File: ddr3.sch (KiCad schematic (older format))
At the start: 61 parts, among them U7 AS4C256M16D3, U8 TPS51200DRC

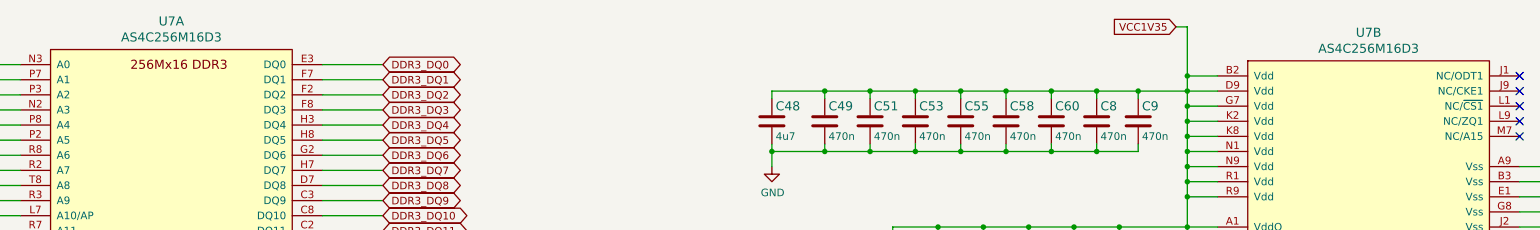
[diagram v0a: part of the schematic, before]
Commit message: Update DDR3 length tunning
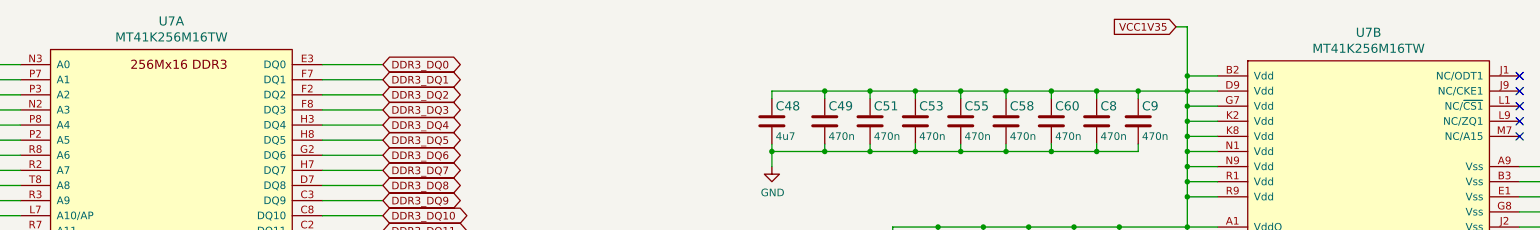
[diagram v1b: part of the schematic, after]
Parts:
- U7: value AS4C256M16D3 -> MT41K256M16TW
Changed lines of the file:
@@
 P 5050 4075
 F 0 "U7" H 5050 5812 60  0000 C CNN
-F 1 "AS4C256M16D3" H 5050 5706 60  0000 C CNN
+F 1 "MT41K256M16TW" H 5050 5706 60  0000 C CNN
 F 2 "artix-dc-scm-footprints:BGA-96_9.0x13.0mm_Layout2x3x16_P0.8mm" H 5050 4075 60  0001 C CNN
 F 3 "" H 5050 4075 60  0001 C CNN
+F 4 "" H 5050 4075 50  0001 C CNN "Field4"
 	1    5050 4075
 	1    0    0    -1
@@
 P 12975 4050
 F 0 "U7" H 12975 5687 60  0000 C CNN
-F 1 "AS4C256M16D3" H 12975 5581 60  0000 C CNN
+F 1 "MT41K256M16TW" H 12975 5581 60  0000 C CNN
 F 2 "artix-dc-scm-footprints:BGA-96_9.0x13.0mm_Layout2x3x16_P0.8mm" H 12975 4050 60  0001 C CNN
 F 3 "" H 12975 4050 60  0001 C CNN

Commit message: Fix USB3300 circuit
-remove 1V8 connection
-add capacitance at internal 1v8 regulators
-apply changes to PCB
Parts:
- C1: footprint artix-dc-scm-footprints:0402-res -> _autosave-artix-dc-scm-footprints:0402-res; symbol artix-dc-scm:C_1n_0402 -> _autosave-artix-dc-scm:C_1n_0402
- C155, C40, C41, C43, C47: footprint artix-dc-scm-footprints:0402-cap -> _autosave-artix-dc-scm-footprints:0402-cap; symbol artix-dc-scm:C_10u_0402 -> _autosave-artix-dc-scm:C_10u_0402
- C42, C44, C46, C57, C62, C63: footprint artix-dc-scm-footprints:0402-cap -> _autosave-artix-dc-scm-footprints:0402-cap; symbol artix-dc-scm:C_100n_0402-artix-dc-scm -> _autosave-artix-dc-scm:C_100n_0402-artix-dc-scm
- C48: footprint artix-dc-scm-footprints:0402-cap -> _autosave-artix-dc-scm-footprints:0402-cap; symbol artix-dc-scm:C_4u7_0402 -> _autosave-artix-dc-scm:C_4u7_0402
- C49, C50, C51, C52, C53, C54, C55, C56, C58, C59, C60, C61, C8, C9: footprint artix-dc-scm-footprints:0402-cap -> _autosave-artix-dc-scm-footprints:0402-cap; symbol artix-dc-scm:C_470n_0402 -> _autosave-artix-dc-scm:C_470n_0402
- R100, R162, R163, R164, R167, R168, R169, R170, R171, R172, R173, R174, R175, R176, R177, R178, R179, R180, R181, R182, R183, R184, R54, R55, R56, R99: footprint artix-dc-scm-footprints:0402-res -> _autosave-artix-dc-scm-footprints:0402-res; symbol artix-dc-scm:R_51R_0402 -> _autosave-artix-dc-scm:R_51R_0402
- R113, R57, R58, R59: footprint artix-dc-scm-footprints:0402-res -> _autosave-artix-dc-scm-footprints:0402-res; symbol artix-dc-scm:R_10k_0402 -> _autosave-artix-dc-scm:R_10k_0402
- R13: footprint artix-dc-scm-footprints:0402-res -> _autosave-artix-dc-scm-footprints:0402-res; symbol artix-dc-scm:R_4k7_0402 -> _autosave-artix-dc-scm:R_4k7_0402
- R60: footprint artix-dc-scm-footprints:0402-res -> _autosave-artix-dc-scm-footprints:0402-res; symbol artix-dc-scm:R_240R_0402 -> _autosave-artix-dc-scm:R_240R_0402
- U7: footprint artix-dc-scm-footprints:BGA-96_9.0x13.0mm_Layout2x3x16_P0.8mm -> _autosave-artix-dc-scm-footprints:BGA-96_9.0x13.0mm_Layout2x3x16_P0.8mm; symbol artix-dc-scm:AS4C256M16D3 -> _autosave-artix-dc-scm:AS4C256M16D3
- U8: footprint artix-dc-scm-footprints:VSON-10-1EP_3x3mm -> _autosave-artix-dc-scm-footprints:VSON-10-1EP_3x3mm; symbol artix-dc-scm:TPS51200DRC -> _autosave-artix-dc-scm:TPS51200DRC

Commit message: Fixed libs
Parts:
- C1: footprint _autosave-artix-dc-scm-footprints:0402-res -> artix-dc-scm-footprints:0402-res; symbol _autosave-artix-dc-scm:C_1n_0402 -> artix-dc-scm:C_1n_0402
- C155, C40, C41, C43, C47: footprint _autosave-artix-dc-scm-footprints:0402-cap -> artix-dc-scm-footprints:0402-cap; symbol _autosave-artix-dc-scm:C_10u_0402 -> artix-dc-scm:C_10u_0402
- C42, C44, C46, C57, C62, C63: footprint _autosave-artix-dc-scm-footprints:0402-cap -> artix-dc-scm-footprints:0402-cap; symbol _autosave-artix-dc-scm:C_100n_0402-artix-dc-scm -> artix-dc-scm:C_100n_0402-artix-dc-scm
- C48: footprint _autosave-artix-dc-scm-footprints:0402-cap -> artix-dc-scm-footprints:0402-cap; symbol _autosave-artix-dc-scm:C_4u7_0402 -> artix-dc-scm:C_4u7_0402
- C49, C50, C51, C52, C53, C54, C55, C56, C58, C59, C60, C61, C8, C9: footprint _autosave-artix-dc-scm-footprints:0402-cap -> artix-dc-scm-footprints:0402-cap; symbol _autosave-artix-dc-scm:C_470n_0402 -> artix-dc-scm:C_470n_0402
- R100, R162, R163, R164, R167, R168, R169, R170, R171, R172, R173, R174, R175, R176, R177, R178, R179, R180, R181, R182, R183, R184, R54, R55, R56, R99: footprint _autosave-artix-dc-scm-footprints:0402-res -> artix-dc-scm-footprints:0402-res; symbol _autosave-artix-dc-scm:R_51R_0402 -> artix-dc-scm:R_51R_0402
- R113, R57, R58, R59: footprint _autosave-artix-dc-scm-footprints:0402-res -> artix-dc-scm-footprints:0402-res; symbol _autosave-artix-dc-scm:R_10k_0402 -> artix-dc-scm:R_10k_0402
- R13: footprint _autosave-artix-dc-scm-footprints:0402-res -> artix-dc-scm-footprints:0402-res; symbol _autosave-artix-dc-scm:R_4k7_0402 -> artix-dc-scm:R_4k7_0402
- R60: footprint _autosave-artix-dc-scm-footprints:0402-res -> artix-dc-scm-footprints:0402-res; symbol _autosave-artix-dc-scm:R_240R_0402 -> artix-dc-scm:R_240R_0402
- U7: footprint _autosave-artix-dc-scm-footprints:BGA-96_9.0x13.0mm_Layout2x3x16_P0.8mm -> artix-dc-scm-footprints:BGA-96_9.0x13.0mm_Layout2x3x16_P0.8mm; symbol _autosave-artix-dc-scm:AS4C256M16D3 -> artix-dc-scm:AS4C256M16D3
- U8: footprint _autosave-artix-dc-scm-footprints:VSON-10-1EP_3x3mm -> artix-dc-scm-footprints:VSON-10-1EP_3x3mm; symbol _autosave-artix-dc-scm:TPS51200DRC -> artix-dc-scm:TPS51200DRC
